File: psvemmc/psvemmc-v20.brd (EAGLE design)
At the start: 38 x 30.5 mm, 43 parts, among them J1 CON_HEADER_2X10-SHROUDED, U1 USB2244QFN, U2 LP3996_DSC_10, U3 TXS02612, X1 ZX62D-B-5PA8, Y1 XRCGB

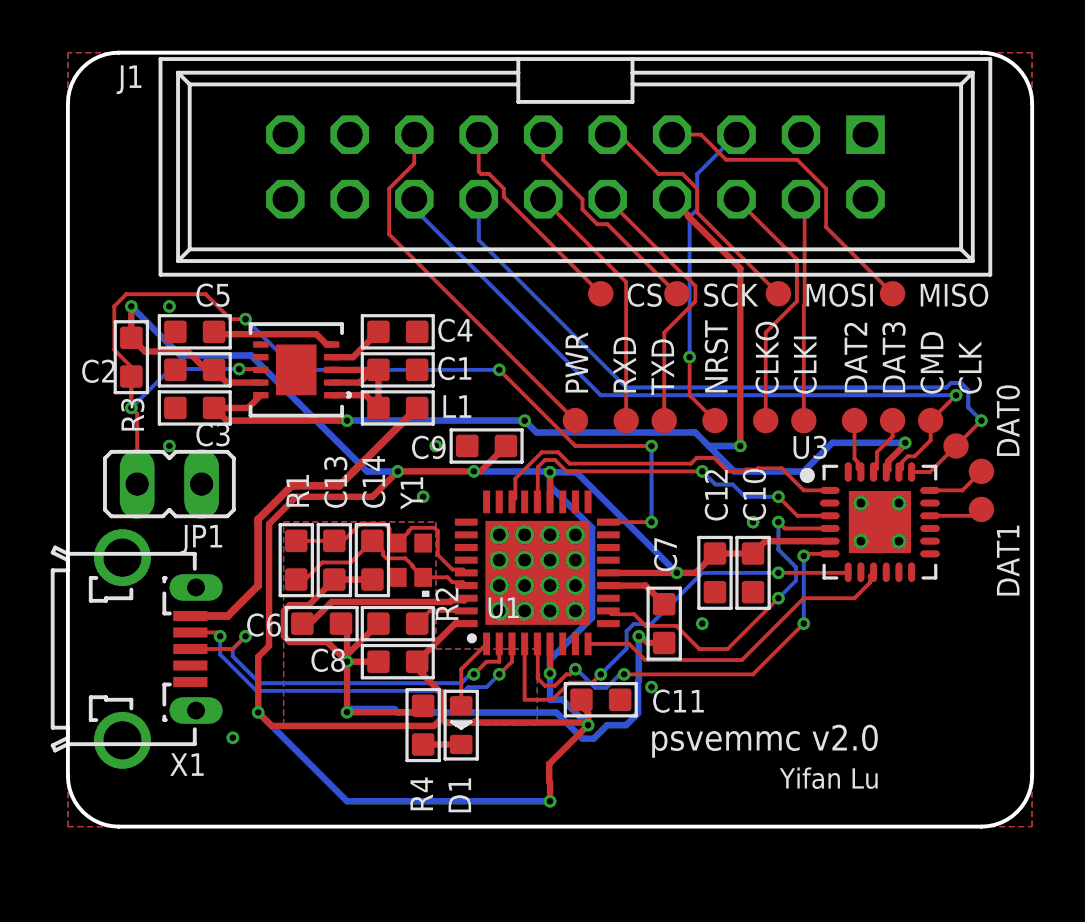
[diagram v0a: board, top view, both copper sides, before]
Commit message: psvemmc v2.1: added EEPROM and GND pad
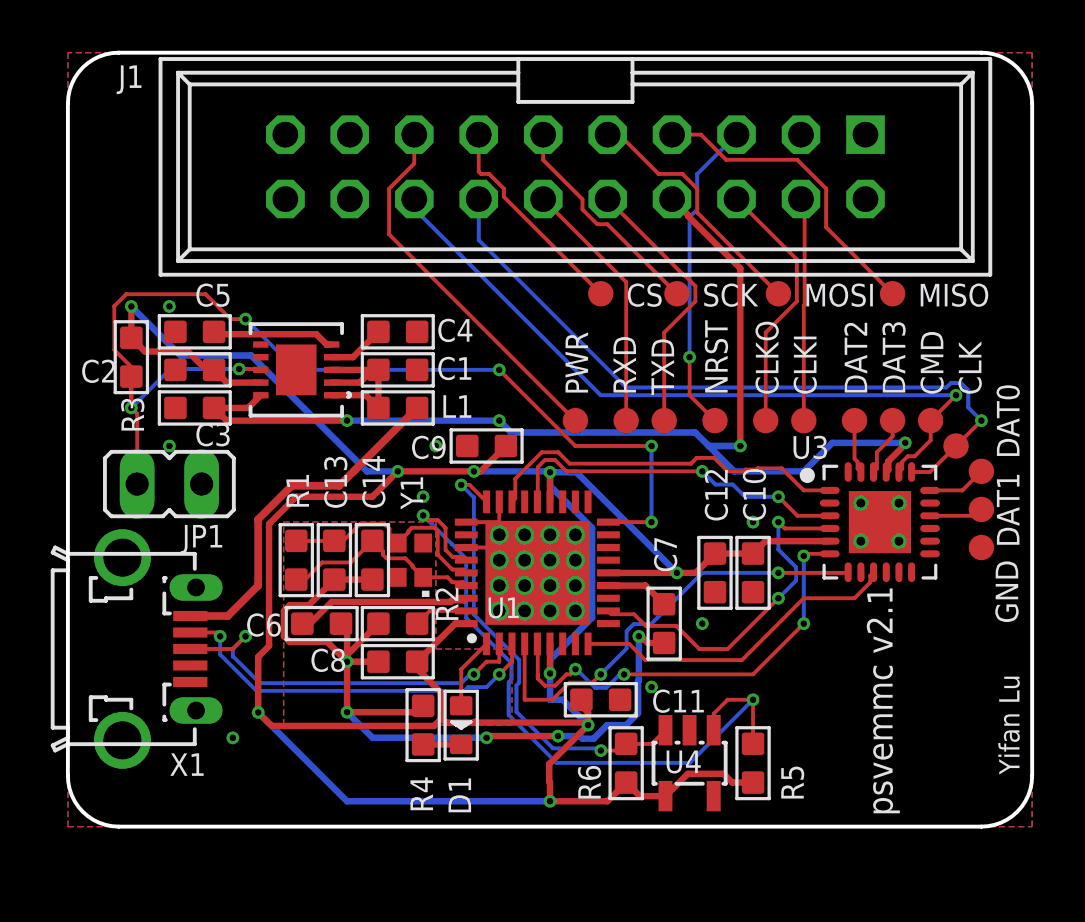
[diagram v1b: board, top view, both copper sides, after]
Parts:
- added GND: TPTP10R, testpad:TP10R
- added R5, R6: 10K, Seeed-Resistor:R0603
- added U4: 24AA00OT, microchip:SOT23-5L
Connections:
- new net IC_SCK: R5.1, U1.31, U4.1
- new net IC_SDA: R6.1, U1.27, U4.3
- net GND: now also GND.TP, U4.2
- net VDD33: now also R5.2, R6.2, U4.4
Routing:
- net IC_SCK: track 0.00 -> 27.9 mm, vias 0 -> 2
- net IC_SDA: track 0.00 -> 18.1 mm, vias 0 -> 2
- net VDD33: track 108.6 -> 117.7 mm
- net GND: track 38.6 -> 42.2 mm, vias 31 -> 33
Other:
- board text added: "psvemmc v2.1"
- board text removed: "psvemmc v2.0"
